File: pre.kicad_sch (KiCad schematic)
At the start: 56 parts, among them J3 Conn_01x03, J4 Conn_01x03, Q2 BSS138, U1 TL072, U2 TL074

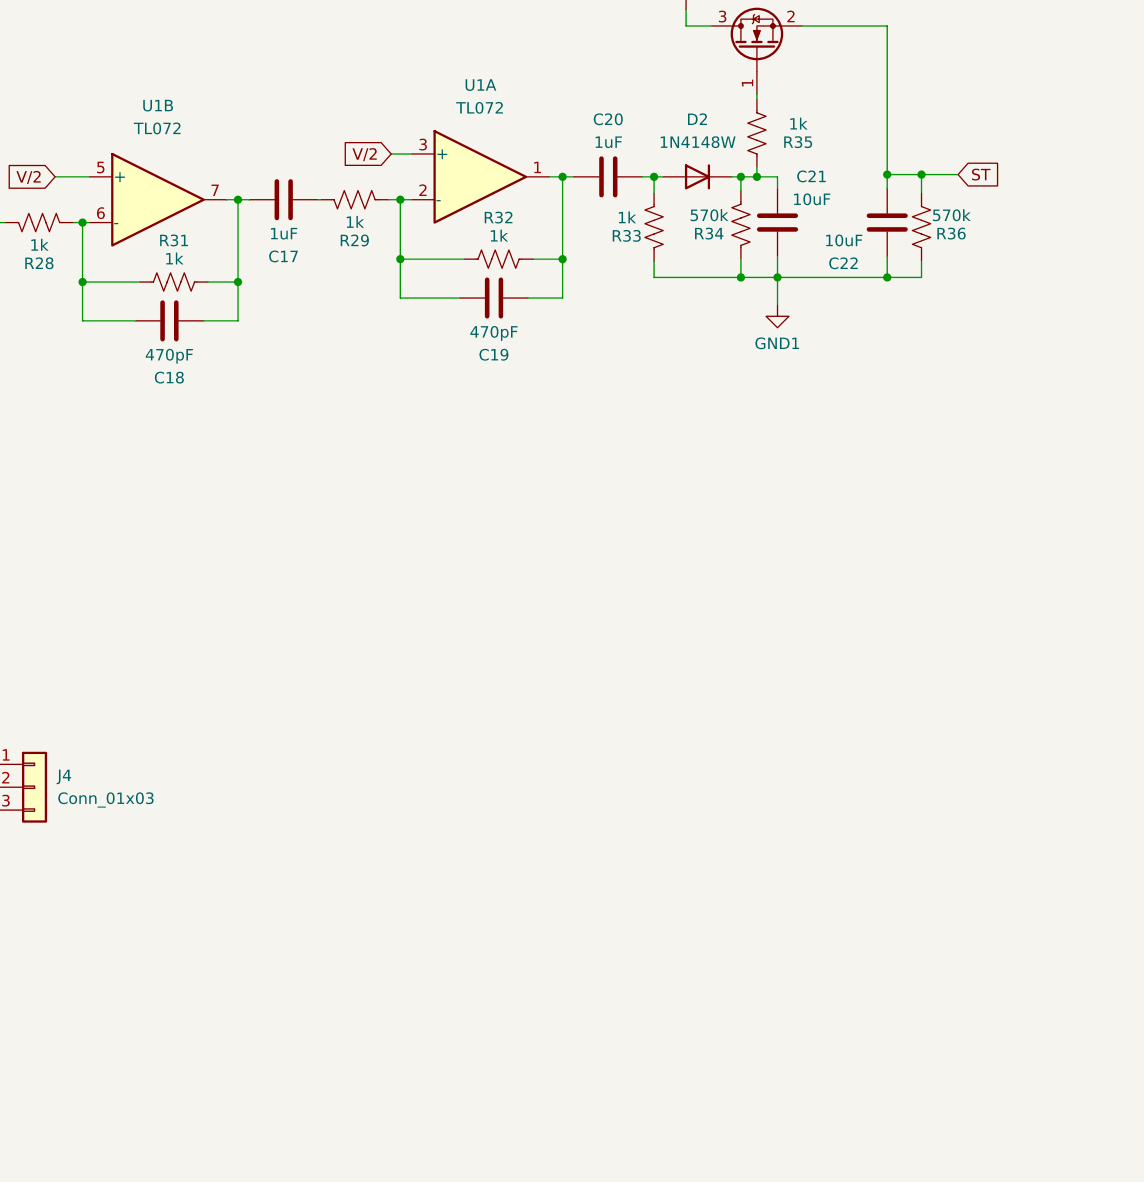
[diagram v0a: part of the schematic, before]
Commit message: correcao de standby no IC
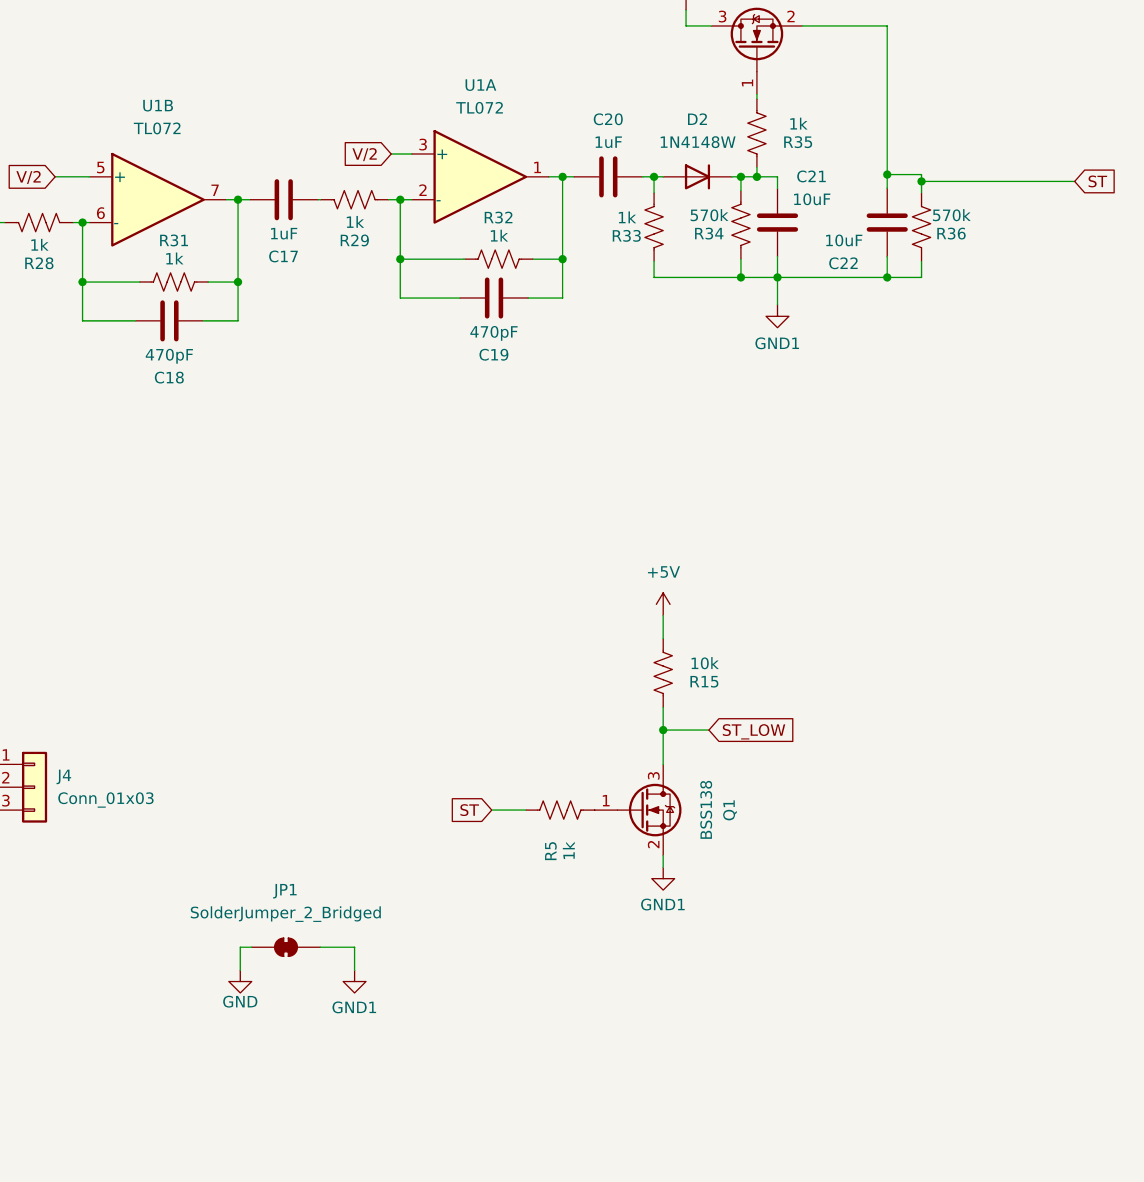
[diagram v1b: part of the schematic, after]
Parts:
- added JP1: SolderJumper_2_Bridged, Jumper:SolderJumper-2_P1.3mm_Bridged2Bar_RoundedPad1.0x1.5mm, symbol Jumper:SolderJumper_2_Bridged
- added Q1: BSS138, Package_TO_SOT_SMD:SOT-23, symbol Transistor_FET:BSS138
- added R15: 10k, Resistor_SMD:R_0805_2012Metric, symbol Device:R_US
- added R5: 1k, Resistor_SMD:R_0805_2012Metric, symbol Device:R_US
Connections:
- net GND1: now also JP1.2 (B), Q1.2 (S)
- net ST: now also R5.2
- new net: Q1.1 (G), R5.1
- new net +5V: R15.1
- new net GND: JP1.1 (A)
- new net ST_LOW: Q1.3 (D), R15.2

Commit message: v2.0 pre APL_STA2150
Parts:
- removed J3, J4: Conn_01x03, Connector_JST:JST_XH_B3B-XH-A_1x03_P2.50mm_Vertical, symbol Connector_Generic:Conn_01x03
- removed R10, R6, R7, R8, R9: 100k, Resistor_SMD:R_0805_2012Metric, symbol Device:R_US
- added C10, C25, C27, C28: 100nf, Capacitor_SMD:C_0805_2012Metric, symbol Device:C
- added C8, C9: 2.2uF, Capacitor_SMD:C_0805_2012Metric, symbol Device:C
- added J4: Conn_01x01, Connector_PinHeader_2.54mm:PinHeader_1x01_P2.54mm_Vertical, symbol Connector_Generic:Conn_01x01
- added J5: Conn_01x03, Connector_JST:JST_XH_B3B-XH-A_1x03_P2.50mm_Vertical, symbol Connector_Generic:Conn_01x03
- added J6, J7: Conn_01x04, Connector_JST:JST_XH_B4B-XH-A_1x04_P2.50mm_Vertical, symbol Connector_Generic:Conn_01x04
- added U3: TL072, Package_SO:SOIC-8_3.9x4.9mm_P1.27mm, symbol Amplifier_Operational:TL072
- C13: value 2.2uF -> 100nf
- C14, C15: value 470pF -> 33pF
- C22: value 10uF -> X
- C23: value 10uF -> 2.2uF
- R19, R21: value 100k -> 10k
- R22, R24, R32: value 1k -> 10k
- R23, R25, R31: value 1k -> 100k
- R3: value 100k -> 10
- R34: value 570k -> 10k
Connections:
- net +12V: no longer C23.1, C24.1, C5.1, R19.1, R3.1, U1.8 (V+), U2.4 (V+)
- net +5V: now also R3.1
- net BT_L: now also J6.3 (Pin_3)
- net BT_R: now also C1.1, J6.1 (Pin_1); no longer C1.2
- net GND1: now also C23.1, C10.1, C25.2, C27.2, C28.2, C8.2, C9.2, J5.2 (Pin_2), J6.2 (Pin_2), J7.2 (Pin_2), U3.4 (V-); no longer C23.2
- net V/2: now also C25.1, C27.1, C28.1, U3.6 (-), U3.7; no longer R20.2
- net at R3.2: now also C23.2, C24.1, C5.1, R19.1, U1.8 (V+), U2.4 (V+), C8.1, C9.1, U3.8 (V+)
- net at R19.2, R20.1, R21.1: no longer C13.1
- net V/2_AUDIO: now reaches U2.3 (+)
- net V/2_AUDIO: now also C13.1, U2.5 (+), U3.1, U3.2 (-), U3.5 (+)
- net at C2.2: now also J5.3 (Pin_3), J7.3 (Pin_3)
- net at C11.1, R13.1: now also C1.2; no longer C1.1
- net at C4.2: now also J5.1 (Pin_1), J7.1 (Pin_1)
- new net: C10.2, R20.2, U3.3 (+)
- new net ST_OUT: J4.1 (Pin_1), J6.4 (Pin_4), J7.4 (Pin_4)
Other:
- moved on the sheet: C1, C14, C15, C16, C17, C18, C19, C2, C20, C21, C22, C24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
